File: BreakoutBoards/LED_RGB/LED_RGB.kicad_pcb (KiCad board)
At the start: 2 copper layers, 11.3 x 12.8 mm, 7 parts, among them J1 Conn_01x04_Pin

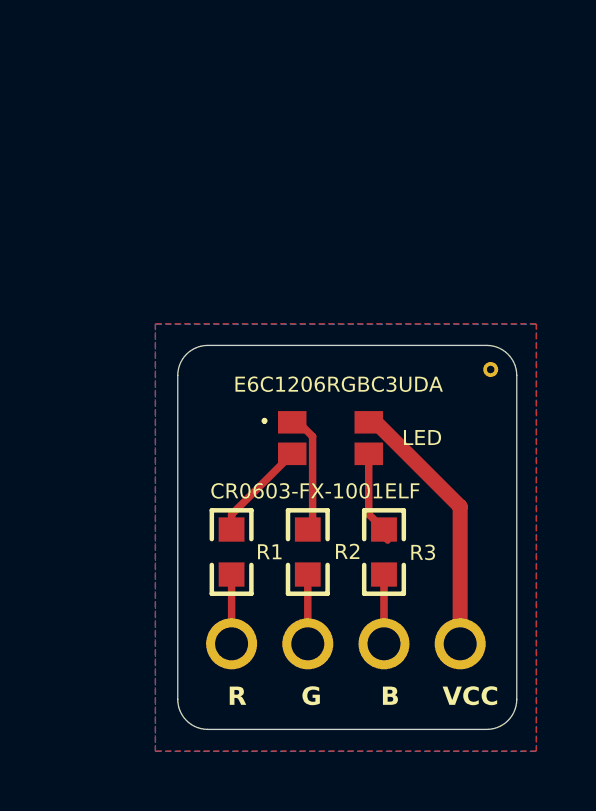
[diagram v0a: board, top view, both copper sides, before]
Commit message: replaced out of stock resistors
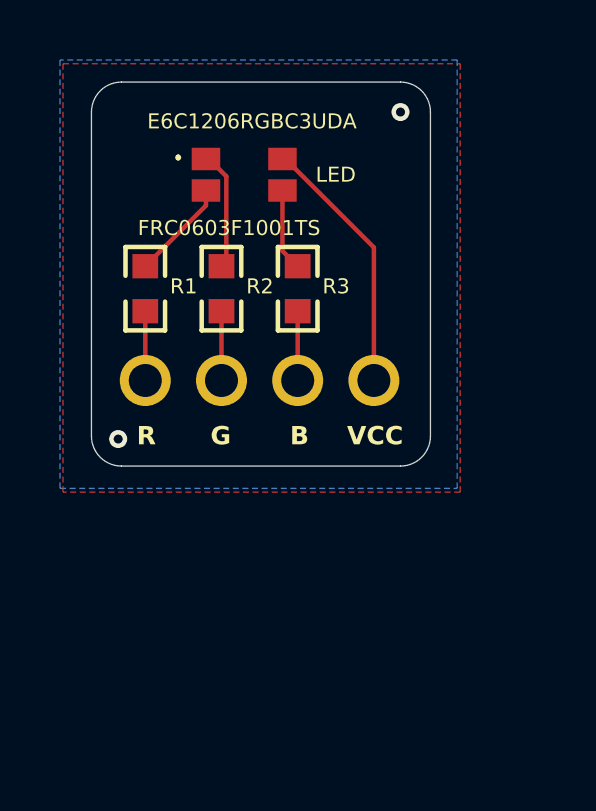
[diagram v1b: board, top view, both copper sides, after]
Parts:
- removed TP1: TestPoint, TestPoint:TestPoint_THTPad_D1.0mm_Drill0.5mm
- J1: value Conn_01x04_Pin -> HDR-TH_4P-P2.54-V-M
- R1, R2, R3: value CR0603-FX-1001ELF -> FRC0603F1001TS
- moved J1 9.24 mm to (94.9, 88.8)
- moved R1 9.24 mm to (91.1, 85.7)
- moved R2 9.24 mm to (93.6, 85.7)
- moved R3 9.24 mm to (96.2, 85.7)
- moved LED1 9.24 mm to (94.4, 81.9)
- moved G*** 9.05 mm to (94.9, 81.3)
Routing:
- net GND: vias 0 -> 2
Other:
- board text added: "Charge LED_RGB Mk 0.1"
- board text added: "FRC0603F1001TS"
- board text removed: "CR0603-FX-1001ELF"
- board text removed: "ChargeForge LED_RGB Mk 0.1"
